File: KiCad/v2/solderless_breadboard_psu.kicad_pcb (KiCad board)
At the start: 4 copper layers, 77 parts, among them IC201 TPS63000DRCR, IC202 TPS63000DRCR, IC301 CP2102N-A02-GQFN24R, J201 Barrel_Jack_Switch_Pin3Ring, J202 Conn_01x03_Pin, J203 Conn_02x03_Odd_Even, J204 Conn_01x03_Pin, J205 Conn_02x03_Odd_Even, J301 Conn_01x09_Pin, J302 Conn_01x09_Pin, J303 Conn_01x06_Pin, J304 USB_C_Receptacle_USB2.0_16P, J305 Conn_01x03_Pin, U301 USBLC6-2SC6

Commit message: Scheme updates
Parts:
- added FB203: 120R, Fuse:Fuse_0603_1608Metric, F.Cu at (130.8, 156.0)
- added FB204: 120R, Fuse:Fuse_0603_1608Metric, F.Cu at (43.3, 169.2)
- added SW301: ~, psu:SW_PUSH_6mm_H5mm, F.Cu at (107.0, 130.5)
- moved FB202 54.9 mm to (77.8, 170.2), turned to 90 degrees
- moved C203 4.78 mm to (66.7, 170.2)
- moved C204 4.78 mm to (71.5, 175.4)
- moved C205 4.78 mm to (76.0, 170.2)
- moved C206 4.78 mm to (74.2, 170.2)
- moved C207 4.78 mm to (67.5, 175.4)
- moved D202 4.78 mm to (76.0, 174.4)
- moved IC201 4.78 mm to (70.5, 170.4)
- moved L201 4.78 mm to (70.5, 163.8)
- moved R201 4.78 mm to (74.5, 174.4)
- moved R202 4.78 mm to (67.5, 173.9)
- moved R203 4.78 mm to (72.5, 173.9)
- moved R204 4.78 mm to (70.5, 173.9)
- moved C210 2.95 mm to (32.0, 169.8)
- moved R206 2.95 mm to (32.5, 173.2)
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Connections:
- C204 pad 1: +5V -> /[2] Power/5V_OUT
- C205 pad 1: +5V -> /[2] Power/5V_OUT
- C206 pad 1: +5V -> /[2] Power/5V_OUT
- C211 pad 1: +3V3 -> /[2] Power/3V3_OUT
- C212 pad 1: +3V3 -> /[2] Power/3V3_OUT
- C213 pad 1: +3V3 -> /[2] Power/3V3_OUT
- FB202 pad 1: +5V_IN_FILT -> +5V
- FB202 pad 2: +5V_IN_FUSE -> /[2] Power/5V_OUT
- IC201 pad 1: +5V -> /[2] Power/5V_OUT
- IC202 pad 1: +3V3 -> /[2] Power/3V3_OUT
- R203 pad 1: +5V -> /[2] Power/5V_OUT
- R207 pad 1: +3V3 -> /[2] Power/3V3_OUT

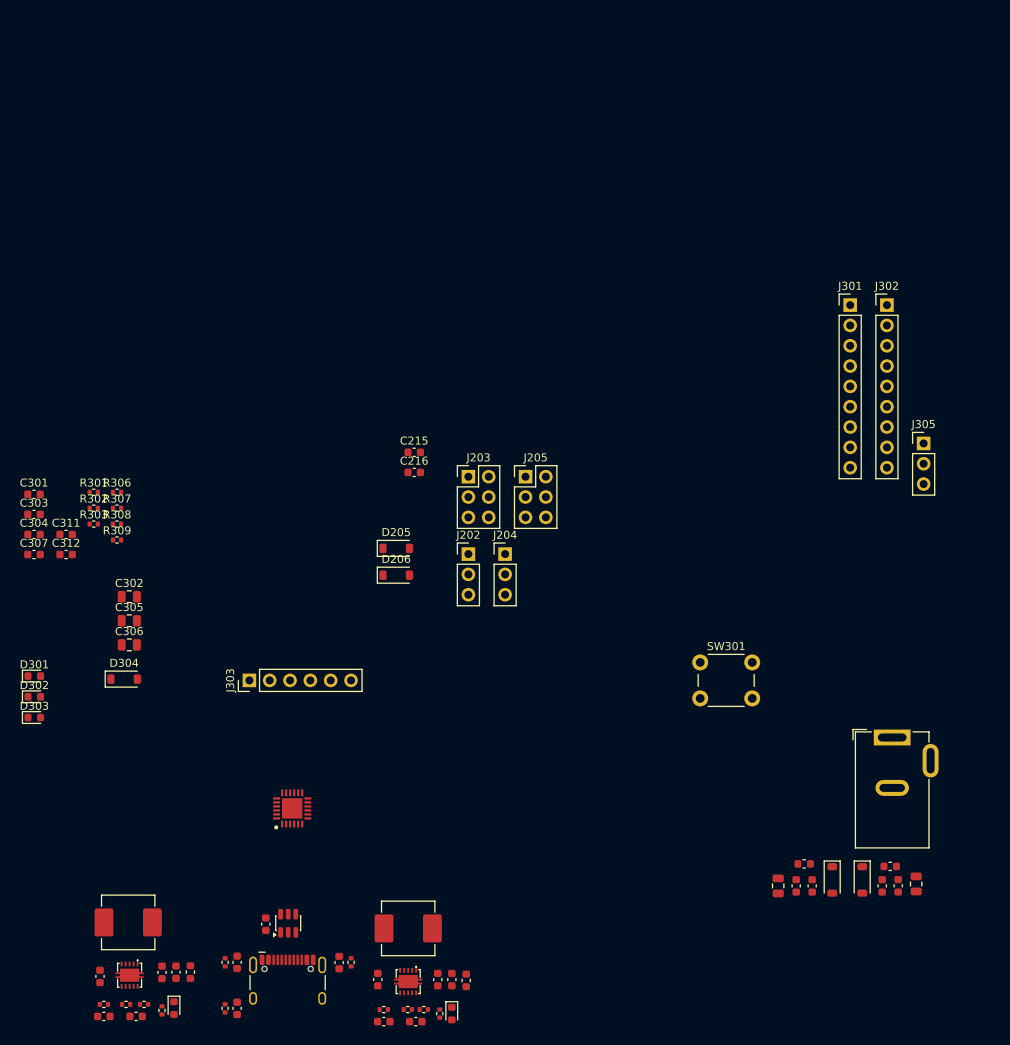
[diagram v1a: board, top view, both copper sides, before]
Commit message: update FB capacitors
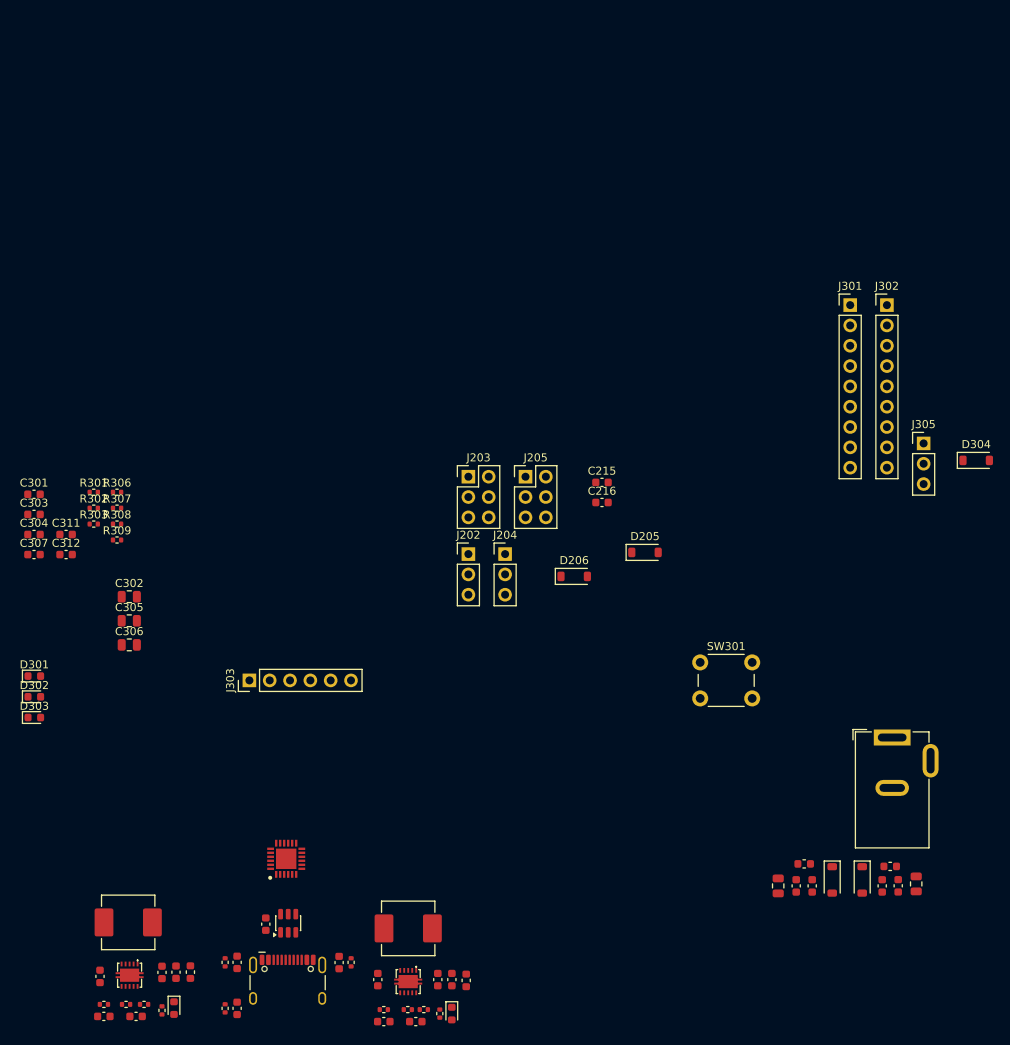
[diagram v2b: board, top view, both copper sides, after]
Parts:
- C204: value 30pF -> 2.4pF
- C211: value 30pF -> 4pF
- moved D304 110.0 mm to (141.5, 105.2)
- moved D205 31.1 mm to (100.1, 116.8)
- moved C215 23.8 mm to (94.7, 108.0)
- moved C216 23.8 mm to (94.7, 110.5)
- moved D206 22.3 mm to (91.2, 119.8)
- moved IC301 6.34 mm to (55.2, 155.1)
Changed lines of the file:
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@@
 	(footprint "Capacitor_SMD:C_0603_1608Metric"
 		(layer "F.Cu")
-		(at 71.25 104.24)
+		(at 94.725 108)
 		(descr "Capacitor SMD 0603 (1608 Metric), square (rectangular) end terminal, IPC-7351 nominal, (Body size source: IPC-SM-782 page 76, https://www.pcb-3d.com/wordpress/wp-content/uploads/ipc-sm-782a_amendment_1_and_2.pdf), generated with kicad-footprint-generator")
 		(tags "capacitor")
@@
 	(footprint "Diode_SMD:D_SOD-123"
 		(layer "F.Cu")
-		(at 34.99 132.59)
+		(at 141.5 105.25)
 		(descr "SOD-123")
 		(tags "SOD-123")
@@
 			)
 		)
-		(property "Value" "30pF"
+		(property "Value" "2.4pF"
 			(at 0 1.43 0)
 			(layer "F.Fab")
@@
 	(footprint "psu:QFN50P400X400X80-25N-D"
 		(layer "F.Cu")
-		(at 56 148.75 90)
+		(at 55.25 155.05 90)
 		(descr "24-Pin QFN-1")
 		(tags "Integrated Circuit")
@@
 			)
 		)
-		(property "Value" "30pF"
+		(property "Value" "4pF"
 			(at 0 1.43 0)
 			(layer "F.Fab")
@@
 	(footprint "Diode_SMD:D_SOD-123"
 		(layer "F.Cu")
-		(at 69 119.6)
+		(at 91.25 119.75)
 		(descr "SOD-123")
 		(tags "SOD-123")
@@
 	(footprint "Capacitor_SMD:C_0603_1608Metric"
 		(layer "F.Cu")
-		(at 71.25 106.75)
+		(at 94.725 110.51)
 		(descr "Capacitor SMD 0603 (1608 Metric), square (rectangular) end terminal, IPC-7351 nominal, (Body size source: IPC-SM-782 page 76, https://www.pcb-3d.com/wordpress/wp-content/uploads/ipc-sm-782a_amendment_1_and_2.pdf), generated with kicad-footprint-generator")
 		(tags "capacitor")
@@
 	(footprint "Diode_SMD:D_SOD-123"
 		(layer "F.Cu")
-		(at 69 116.25)
+		(at 100.1 116.75)
 		(descr "SOD-123")
 		(tags "SOD-123")

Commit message: Initial components placement
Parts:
- removed C311: 100nF, Capacitor_SMD:C_0603_1608Metric
- removed SW301: ~, psu:SW_PUSH_6mm_H5mm
- C207, C214, C301, C303, C304, C307, C310: footprint Capacitor_SMD:C_0603_1608Metric -> Capacitor_SMD:C_0402_1005Metric
- C302, C305, C306: footprint Capacitor_SMD:C_0805_2012Metric -> Capacitor_SMD:C_0603_1608Metric
- J201: value Barrel_Jack_Switch_Pin3Ring -> Conn_01x02_Pin; footprint Connector_BarrelJack:BarrelJack_GCT_DCJ200-10-A_Horizontal -> Connector_PinHeader_2.54mm:PinHeader_1x02_P2.54mm_Vertical
- moved C214 102.0 mm to (88.8, 89.7), turned to -90 degrees
- moved R206 101.6 mm to (90.2, 89.7), turned to -90 degrees
- moved C210 101.5 mm to (93.8, 89.2), turned to 180 degrees
- moved R205 99.7 mm to (73.2, 80.1)
- moved D204 98.4 mm to (71.5, 80.1)
- moved R208 97.7 mm to (90.2, 92.5), turned to 90 degrees
- moved C211 96.4 mm to (88.8, 93.8), turned to 90 degrees
- moved IC202 96.3 mm to (93.9, 93.0), turned to 180 degrees
- moved L202 95.7 mm to (100.5, 92.8), turned to -90 degrees
- moved D202 94.6 mm to (69.2, 80.0)
- moved R201 94.6 mm to (67.8, 80.0)
- moved R207 94.6 mm to (90.2, 94.8), turned to 90 degrees
- moved C212 91.1 mm to (95.3, 97.0), turned to 0 degrees
- moved IC301 90.2 mm to (77.2, 67.5), turned to 0 degrees
- moved C213 88.2 mm to (92.1, 97.0), turned to 180 degrees
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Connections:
- D206 pad 1: VCC_L -> VCC_R
- J301 pad 7: /[3] USB 2 UART/RS485 -> /[3] USB 2 UART/RSTB
- J301 pad 9: /[3] USB 2 UART/RSTB -> /[3] USB 2 UART/RS485
- U301 pad 1: /[3] USB 2 UART/USB_CONN_D+ -> /[3] USB 2 UART/USB_CONN_D-
- U301 pad 3: /[3] USB 2 UART/USB_CONN_D- -> /[3] USB 2 UART/USB_CONN_D+
- U301 pad 4: USB_D- -> USB_D+
- U301 pad 6: USB_D+ -> USB_D-
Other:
- board outline added: 55 x 51 mm

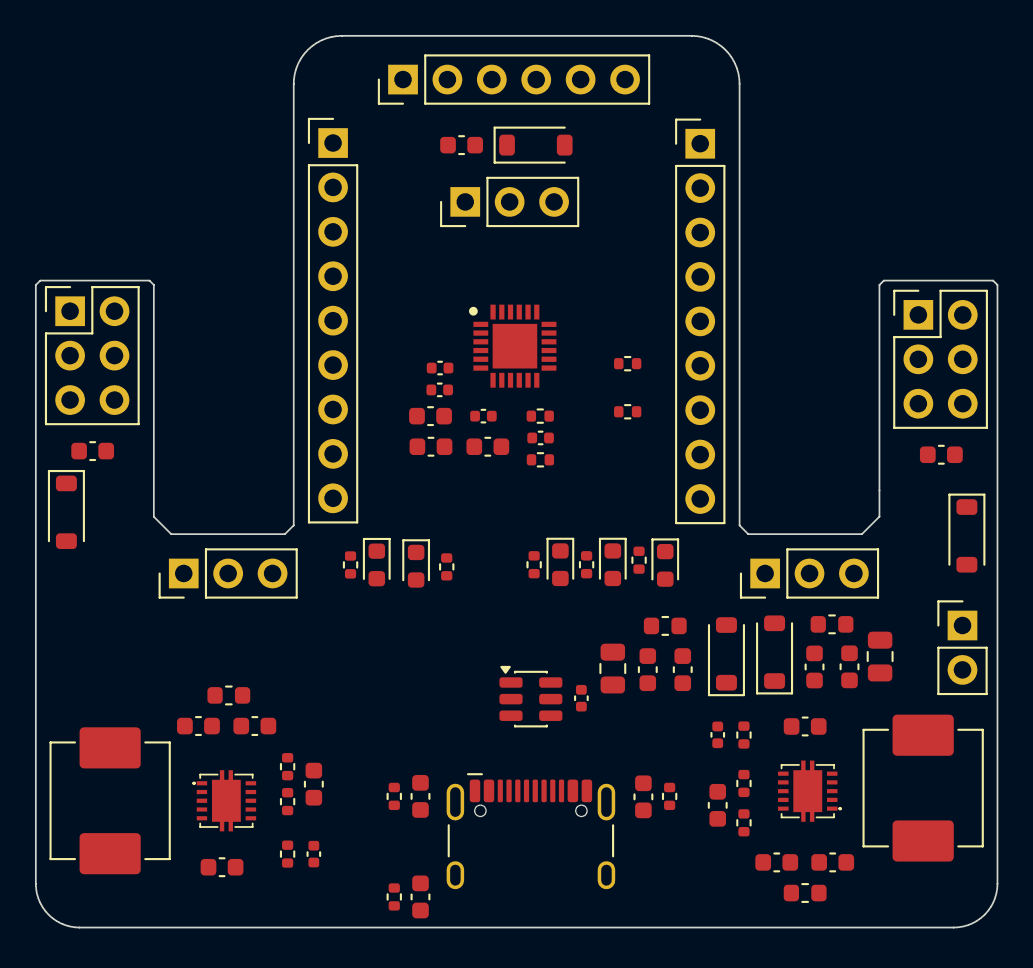
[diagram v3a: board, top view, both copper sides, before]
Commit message: PCB layout updates
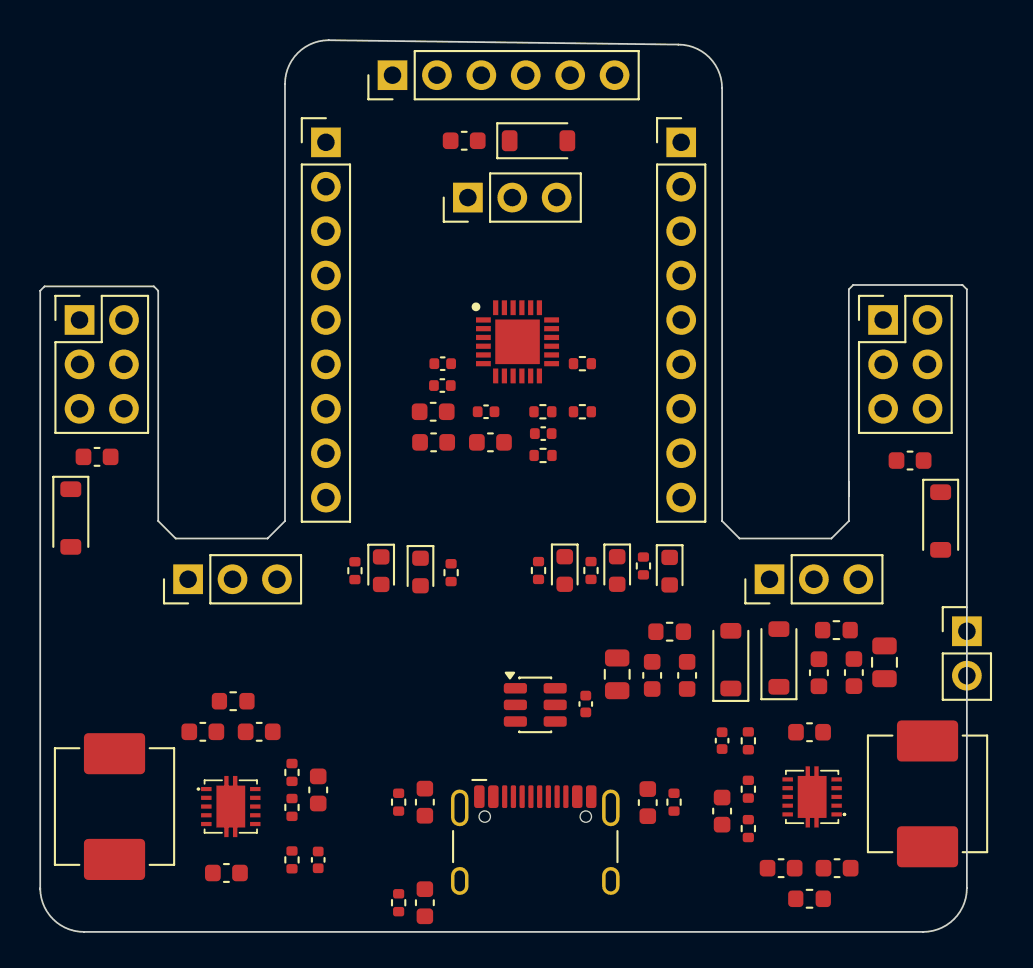
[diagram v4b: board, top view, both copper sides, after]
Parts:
- moved R303 2.59 mm to (81.0, 71.2)
- moved R309 2.59 mm to (81.0, 68.5)
- moved J205 2.04 mm to (98.2, 66.0)
- moved C216 1.82 mm to (99.8, 74.0)
- moved D206 1.72 mm to (101.5, 77.5)
- moved J301 1.09 mm to (86.7, 55.8)
- moved J203 0.74 mm to (52.2, 66.0)
- moved J303 0.65 mm to (70.2, 52.0)
- moved C205 0.41 mm to (59.3, 89.6)
- moved C206 0.41 mm to (62.5, 89.6)
- moved D201 0.41 mm to (89.5, 85.4)
- moved D204 0.41 mm to (71.8, 80.4)
- moved D301 0.41 mm to (86.0, 80.4)
- moved FB202 0.41 mm to (61.0, 87.8)
- moved J201 0.41 mm to (103.0, 83.8)
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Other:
- board size 55 x 51 mm -> 53 x 51 mm

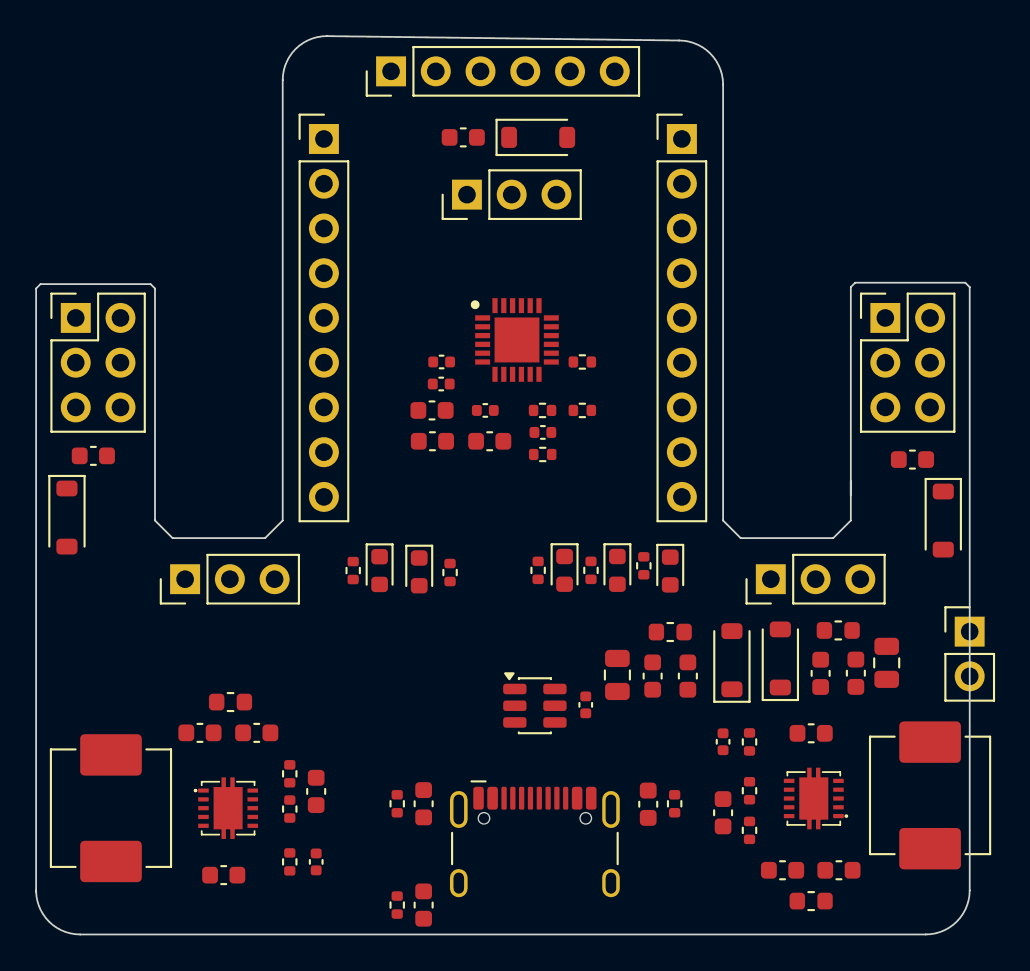
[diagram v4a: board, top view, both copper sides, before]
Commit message: board outline fix
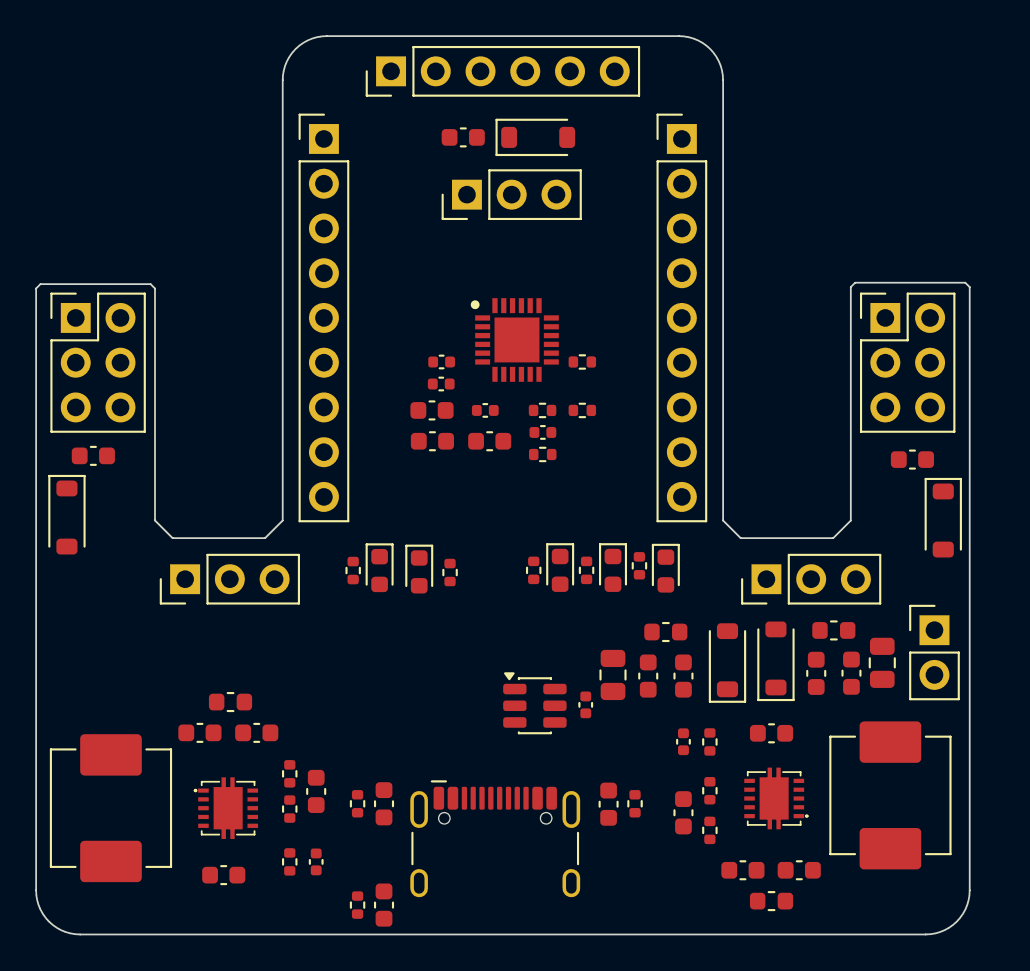
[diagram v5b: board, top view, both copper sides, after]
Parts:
- moved C210 2.25 mm to (91.8, 89.6)
- moved C211 2.25 mm to (86.8, 94.1)
- moved C212 2.25 mm to (93.3, 97.4)
- moved C213 2.25 mm to (90.1, 97.4)
- moved C214 2.25 mm to (86.8, 90.1)
- moved C308 2.25 mm to (82.5, 93.6)
- moved C309 2.25 mm to (69.8, 93.6)
- moved C313 2.25 mm to (69.8, 99.3)
- moved FB204 2.25 mm to (91.8, 99.1)
- moved IC202 2.25 mm to (91.9, 93.3)
- moved J304 2.25 mm to (76.1, 97.0)
- moved L202 2.25 mm to (98.5, 93.1)
- moved R206 2.25 mm to (88.2, 90.1)
- moved R207 2.25 mm to (88.2, 95.1)
- moved R208 2.25 mm to (88.2, 92.8)
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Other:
- outline, holes or cut-outs redrawn

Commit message: initial routing
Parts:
- moved D201 24.0 mm to (65.2, 86.0)
- moved D301 20.5 mm to (74.5, 63.2)
- moved C202 19.3 mm to (67.5, 87.0)
- moved D302 17.6 mm to (78.5, 63.2)
- moved D303 17.4 mm to (76.5, 63.2)
- moved FB201 17.3 mm to (68.5, 84.5), turned to 0 degrees
- moved R306 17.1 mm to (74.5, 66.0), turned to 90 degrees
- moved C201 15.3 mm to (69.5, 87.0)
- moved R308 14.6 mm to (78.5, 66.0), turned to 90 degrees
- moved R307 14.4 mm to (76.5, 66.0), turned to 90 degrees
- moved C313 14.1 mm to (83.8, 98.0), turned to 0 degrees
- moved R301 13.1 mm to (86.5, 81.8), turned to 180 degrees
- moved F201 11.3 mm to (71.5, 86.8)
- moved C303 11.1 mm to (86.5, 80.5), turned to 0 degrees
- moved C302 10.4 mm to (82.2, 76.8), turned to -90 degrees
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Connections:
- U301 pad 1: /[3] USB 2 UART/USB_CONN_D- -> /[3] USB 2 UART/USB_CONN_D+
- U301 pad 3: /[3] USB 2 UART/USB_CONN_D+ -> /[3] USB 2 UART/USB_CONN_D-
- U301 pad 4: USB_D+ -> USB_D-
- U301 pad 6: USB_D- -> USB_D+
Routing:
- net +5V_IN: track 0.00 -> 73.7 mm, vias 0 -> 2
- net GND: track 0.00 -> 31.6 mm, vias 0 -> 69
- net GNDPWR: track 0.00 -> 21.4 mm
- net VBUS_CONN: track 0.00 -> 20.8 mm, vias 0 -> 2
- net USB_D-: track 0.00 -> 13.0 mm
- net USB_D+: track 0.00 -> 13.0 mm
- net +5V_BJ: track 0.00 -> 12.6 mm
- net /[2] Power/5V_OUT: track 0.00 -> 12.5 mm
- net VUSB: track 0.00 -> 10.6 mm
- net VCC_L: track 0.00 -> 10.3 mm
- net /[3] USB 2 UART/USB_CONN_CC2: track 0.00 -> 9.16 mm
- net /[3] USB 2 UART/USB_CONN_D+: track 0.00 -> 8.94 mm, vias 0 -> 2
- net /[3] USB 2 UART/USB_CONN_CC1: track 0.00 -> 8.73 mm
- net +5V: track 0.00 -> 8.72 mm
- net /[3] USB 2 UART/USB_CONN_D-: track 0.00 -> 8.70 mm, vias 0 -> 2
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- added copper zone on F.Cu, net /[2] Power/5V_L1
- added copper zone on F.Cu, net /[2] Power/5V_L2
- added copper zone on B.Cu, net GND
- added copper zone on F.Cu, net GND
- added copper zone on In1.Cu, net GND
- added copper zone on In2.Cu, net GND
